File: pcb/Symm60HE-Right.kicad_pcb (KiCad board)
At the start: 2 copper layers, 157.9 x 105.9 mm, 114 parts

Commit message: Rename to Symm60HE; two-layer routing that is clean by construction
Rename every DOE60-* file and reference to Symm60HE-*, matching the repo.
The seven "DOE" mentions that remain are about the layout being reproduced,
which is correct.

Routing is now two layers with vias, at 0.2 mm trace / 0.15 mm clearance /
0.45 mm vias -- a rule chosen so the 0.5 mm grid's own diagonal spacing
(0.354 mm) satisfies it, and relaxed for any fabricator.

Three fixes, each of which was a real defect in the single-layer pass:

  * A diagonal step now requires both of its orthogonal neighbours.  Without
    it two nets cut the same gap from opposite corners and cross; cell
    ownership cannot see that, because neither net owns a cell the other
    used.  It was producing 49 shorts on the left half alone.
  * Fine-pitch pins are met head-on through a private escape lane along the
    pad's own axis, staggered near/far by pin parity.  A 0.65 mm TSSOP has
    0.25 mm between pads, so there is no side access at any rule; and without
    the lane the two neighbours' keep-out margins meet in front of a pin's
    tip and one of them owns the only way out.  The lane runs both ways,
    because an edge connector's contacts face off-board -- that is the way
    the cable goes in -- so its only exit is inwards under its own body.
  * Every route is rebuilt as real geometry and checked against everything
    already on the board before it is kept.  A route that would violate
    clearance is dropped and counted unrouted, so the files on disk are clean
    by construction and the honest number is the routed/unrouted split.

Left 143 of 156 connections, right 151 of 168, daughterboard 15 of 37.

Two things the checks were missing:

  * routecheck.py never tested trace-to-trace clearance, which is exactly
    what the diagonal crossings needed.  It does now, and it no longer counts
    a branch leaving its trunk at a T as a loose end.
  * The USB-C keep-out only existed in the image script -- nothin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
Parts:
- removed AML1, AML2, AML3, AML4: SN74LV4051A, DOE60_Project:AM1_TSSOP-16_4.4x5mm_P0.65mm
- removed CL10A, CL11A, CL12A, CL13A, CL14A, CL15A, CL16A, CL17A, CL18A, CL19A, CL1A, CL20A, CL21A, CL22A, CL23A, CL24A, CL25A, CL26A, CL27A, CL28A, CL29A, CL2A, CL30A, CL31A, CL32A, CL33A, CL3A, CL4A, CL5A, CL6A, CL7A, CL8A, CL9A, CML1, CML2, CML3, CML4: 100n, DOE60_Project:C1_C_0402_1005Metric
- removed CL10B, CL11B, CL12B, CL13B, CL14B, CL15B, CL16B, CL17B, CL18B, CL19B, CL1B, CL20B, CL21B, CL22B, CL23B, CL24B, CL25B, CL26B, CL27B, CL28B, CL29B, CL2B, CL30B, CL31B, CL32B, CL33B, CL3B, CL4B, CL5B, CL6B, CL7B, CL8B, CL9B: 4.7n, DOE60_Project:C1_C_0402_1005Metric
- removed HEL1, HEL10, HEL11, HEL12, HEL13, HEL14, HEL16, HEL17, HEL18, HEL19, HEL2, HEL20, HEL22, HEL23, HEL24, HEL25, HEL26, HEL27, HEL29, HEL3, HEL31, HEL4, HEL5, HEL6, HEL7, HEL9: MT9102ET, DOE60_Project:HE_KEY_1.00u
- removed HEL15: MT9102ET, DOE60_Project:HE_KEY_1.75u
- removed HEL21, HEL33: MT9102ET, DOE60_Project:HE_KEY_2.25u
- removed HEL28, HEL30, HEL32, HEL8: MT9102ET, DOE60_Project:HE_KEY_1.50u
- removed JL1: FFC_12P, DOE60_Project:FFC_12P_1.00mm_TopContact
- removed MHL1, MHL2, MHL3, MHL4: M2, DOE60_Project:MountingHole_2.2mm_M2_Pad
- removed SL1, SL2: STAB_MX, DOE60_Project:STABILIZER_MX_2U
- added AMR1: SN74LV4051A, Symm60HE_Project:AM1_TSSOP-16_4.4x5mm_P0.65mm, B.Cu at (181.7, 63.5)
- added AMR2: SN74LV4051A, Symm60HE_Project:AM1_TSSOP-16_4.4x5mm_P0.65mm, B.Cu at (207.2, 65.0)
- added AMR3: SN74LV4051A, Symm60HE_Project:AM1_TSSOP-16_4.4x5mm_P0.65mm, B.Cu at (245.7, 65.0)
- added AMR4: SN74LV4051A, Symm60HE_Project:AM1_TSSOP-16_4.4x5mm_P0.65mm, B.Cu at (276.7, 53.5)
- added CMR1: 100n, Symm60HE_Project:C1_C_0402_1005Metric, B.Cu at (189.2, 63.5)
- added CMR2: 100n, Symm60HE_Project:C1_C_0402_1005Metric, B.Cu at (218.2, 62.5)
- added CMR3: 100n, Symm60HE_Project:C1_C_0402_1005Metric, B.Cu at (256.2, 62.5)
- added CMR4: 100n, Symm60HE_Project:C1_C_0402_1005Metric, B.Cu at (284.2, 55.5)
- added CR10A: 100n, Symm60HE_Project:C1_C_0402_1005Metric, B.Cu at (255.3, 21.7)
- added CR10B: 4.7n, Symm60HE_Project:C1_C_0402_1005Metric, B.Cu at (268.5, 35.5)
- added CR11A: 100n, Symm60HE_Project:C1_C_0402_1005Metric, B.Cu at (279.1, 21.7)
- added CR11B: 4.7n, Symm60HE_Project:C1_C_0402_1005Metric, B.Cu at (292.4, 35.5)
- added CR12A: 100n, Symm60HE_Project:C1_C_0402_1005Metric, B.Cu at (217.0, 21.9)
- added CR12B: 4.7n, Symm60HE_Project:C1_C_0402_1005Metric, B.Cu at (230.4, 35.5)
- added CR13A: 100n, Symm60HE_Project:C1_C_0402_1005Metric, B.Cu at (196.5, 22.9)
- added CR13B: 4.7n, Symm60HE_Project:C1_C_0402_1005Metric, B.Cu at (210.5, 35.9)
- added CR14A: 100n, Symm60HE_Project:C1_C_0402_1005Metric, B.Cu at (175.1, 24.9)
- added CR14B: 4.7n, Symm60HE_Project:C1_C_0402_1005Metric, B.Cu at (189.7, 37.2)
- added CR15A: 100n, Symm60HE_Project:C1_C_0402_1005Metric, B.Cu at (154.7, 27.2)
- added CR15B: 4.7n, Symm60HE_Project:C1_C_0402_1005Metric, B.Cu at (169.4, 39.4)
- added CR16A: 100n, Symm60HE_Project:C1_C_0402_1005Metric, B.Cu at (232.5, 40.7)
- added CR16B: 4.7n, Symm60HE_Project:C1_C_0402_1005Metric, B.Cu at (245.7, 54.5)
- added CR17A: 100n, Symm60HE_Project:C1_C_0402_1005Metric, B.Cu at (251.5, 40.7)
- added CR17B: 4.7n, Symm60HE_Project:C1_C_0402_1005Metric, B.Cu at (264.7, 54.5)
- added CR18A: 100n, Symm60HE_Project:C1_C_0402_1005Metric, B.Cu at (277.7, 40.7)
- added CR18B: 4.7n, Symm60HE_Project:C1_C_0402_1005Metric, B.Cu at (290.9, 54.5)
- added CR19A: 100n, Symm60HE_Project:C1_C_0402_1005Metric, B.Cu at (213.1, 41.0)
- added CR19B: 4.7n, Symm60HE_Project:C1_C_0402_1005Metric, B.Cu at (226.6, 54.6)
- added CR1A: 100n, Symm60HE_Project:C1_C_0402_1005Metric, B.Cu at (224.8, 2.66)
- added CR1B: 4.7n, Symm60HE_Project:C1_C_0402_1005Metric, B.Cu at (238.1, 16.4)
- added CR20A: 100n, Symm60HE_Project:C1_C_0402_1005Metric, B.Cu at (192.3, 42.2)
- added CR20B: 4.7n, Symm60HE_Project:C1_C_0402_1005Metric, B.Cu at (206.4, 55.1)
- added CR21A: 100n, Symm60HE_Project:C1_C_0402_1005Metric, B.Cu at (170.9, 44.4)
- added CR21B: 4.7n, Symm60HE_Project:C1_C_0402_1005Metric, B.Cu at (185.5, 56.7)
- added CR22A: 100n, Symm60HE_Project:C1_C_0402_1005Metric, B.Cu at (227.7, 59.8)
- added CR22B: 4.7n, Symm60HE_Project:C1_C_0402_1005Metric, B.Cu at (240.9, 73.6)
- added CR23A: 100n, Symm60HE_Project:C1_C_0402_1005Metric, B.Cu at (246.8, 59.8)
- added CR23B: 4.7n, Symm60HE_Project:C1_C_0402_1005Metric, B.Cu at (260.0, 73.6)
- added CR24A: 100n, Symm60HE_Project:C1_C_0402_1005Metric, B.Cu at (265.8, 59.8)
- added CR24B: 4.7n, Symm60HE_Project:C1_C_0402_1005Metric, B.Cu at (279.0, 73.6)
- added CR25A: 100n, Symm60HE_Project:C1_C_0402_1005Metric, B.Cu at (277.7, 59.8)
- added CR25B: 4.7n, Symm60HE_Project:C1_C_0402_1005Metric, B.Cu at (290.9, 73.6)
- added CR26A: 100n, Symm60HE_Project:C1_C_0402_1005Metric, B.Cu at (287.2, 59.8)
- added CR26B: 4.7n, Symm60HE_Project:C1_C_0402_1005Metric, B.Cu at (300.4, 73.6)
- added CR27A: 100n, Symm60HE_Project:C1_C_0402_1005Metric, B.Cu at (208.0, 60.3)
- added CR27B: 4.7n, Symm60HE_Project:C1_C_0402_1005Metric, B.Cu at (221.7, 73.7)
- added CR28A: 100n, Symm60HE_Project:C1_C_0402_1005Metric, B.Cu at (186.9, 61.8)
- added CR28B: 4.7n, Symm60HE_Project:C1_C_0402_1005Metric, B.Cu at (201.2, 74.5)
- added CR29A: 100n, Symm60HE_Project:C1_C_0402_1005Metric, B.Cu at (165.7, 64.0)
- added CR29B: 4.7n, Symm60HE_Project:C1_C_0402_1005Metric, B.Cu at (180.4, 76.3)
- added CR2A: 100n, Symm60HE_Project:C1_C_0402_1005Metric, B.Cu at (243.9, 2.62)
- added CR2B: 4.7n, Symm60HE_Project:C1_C_0402_1005Metric, B.Cu at (257.1, 16.4)
- added CR30A: 100n, Symm60HE_Project:C1_C_0402_1005Metric, B.Cu at (246.8, 78.8)
- added CR30B: 4.7n, Symm60HE_Project:C1_C_0402_1005Metric, B.Cu at (260.0, 92.6)
- added CR31A: 100n, Symm60HE_Project:C1_C_0402_1005Metric, B.Cu at (251.5, 78.8)
- added CR31B: 4.7n, Symm60HE_Project:C1_C_0402_1005Metric, B.Cu at (264.7, 92.6)
- added CR32A: 100n, Symm60HE_Project:C1_C_0402_1005Metric, B.Cu at (265.8, 78.8)
- added CR32B: 4.7n, Symm60HE_Project:C1_C_0402_1005Metric, B.Cu at (279.0, 92.6)
- added CR33A: 100n, Symm60HE_Project:C1_C_0402_1005Metric, B.Cu at (280.1, 78.8)
- added CR33B: 4.7n, Symm60HE_Project:C1_C_0402_1005Metric, B.Cu at (293.3, 92.6)
- added CR34A: 100n, Symm60HE_Project:C1_C_0402_1005Metric, B.Cu at (284.9, 78.8)
- added CR34B: 4.7n, Symm60HE_Project:C1_C_0402_1005Metric, B.Cu at (298.1, 92.6)
- added CR35A: 100n, Symm60HE_Project:C1_C_0402_1005Metric, B.Cu at (208.2, 79.5)
- added CR35B: 4.7n, Symm60HE_Project:C1_C_0402_1005Metric, B.Cu at (221.8, 92.9)
- added CR36A: 100n, Symm60HE_Project:C1_C_0402_1005Metric, B.Cu at (169.7, 82.8)
- added CR36B: 4.7n, Symm60HE_Project:C1_C_0402_1005Metric, B.Cu at (184.3, 95.1)
- added CR3A: 100n, Symm60HE_Project:C1_C_0402_1005Metric, B.Cu at (263.0, 2.62)
- added CR3B: 4.7n, Symm60HE_Project:C1_C_0402_1005Metric, B.Cu at (276.2, 16.4)
- added CR4A: 100n, Symm60HE_Project:C1_C_0402_1005Metric, B.Cu at (272.5, 2.62)
- added CR4B: 4.7n, Symm60HE_Project:C1_C_0402_1005Metric, B.Cu at (285.7, 16.4)
- added CR5A: 100n, Symm60HE_Project:C1_C_0402_1005Metric, B.Cu at (282.0, 2.62)
- added CR5B: 4.7n, Symm60HE_Project:C1_C_0402_1005Metric, B.Cu at (295.2, 16.4)
- added CR6A: 100n, Symm60HE_Project:C1_C_0402_1005Metric, B.Cu at (204.9, 3.29)
- added CR6B: 4.7n, Symm60HE_Project:C1_C_0402_1005Metric, B.Cu at (218.6, 16.6)
- added CR7A: 100n, Symm60HE_Project:C1_C_0402_1005Metric, B.Cu at (183.7, 4.93)
- added CR7B: 4.7n, Symm60HE_Project:C1_C_0402_1005Metric, B.Cu at (198.0, 17.5)
- added CR8A: 100n, Symm60HE_Project:C1_C_0402_1005Metric, B.Cu at (162.6, 7.24)
- added CR8B: 4.7n, Symm60HE_Project:C1_C_0402_1005Metric, B.Cu at (177.3, 19.5)
- added CR9A: 100n, Symm60HE_Project:C1_C_0402_1005Metric, B.Cu at (236.3, 21.7)
- added CR9B: 4.7n, Symm60HE_Project:C1_C_0402_1005Metric, B.Cu at (249.5, 35.5)
- added HER1: MT9102ET, Symm60HE_Project:HE_KEY_1.00u, B.Cu at (231.4, 9.54)
- added HER10: MT9102ET, Symm60HE_Project:HE_KEY_1.00u, B.Cu at (261.9, 28.6)
- added HER11: MT9102ET, Symm60HE_Project:HE_KEY_1.50u, B.Cu at (285.8, 28.6)
- added HER12: MT9102ET, Symm60HE_Project:HE_KEY_1.00u, B.Cu at (223.7, 28.7)
- added HER13: MT9102ET, Symm60HE_Project:HE_KEY_1.00u, B.Cu at (203.5, 29.4)
- added HER14: MT9102ET, Symm60HE_Project:HE_KEY_1.00u, B.Cu at (182.4, 31.1)
- added HER15: MT9102ET, Symm60HE_Project:HE_KEY_1.00u, B.Cu at (162.0, 33.3)
- added HER16: MT9102ET, Symm60HE_Project:HE_KEY_1.00u, B.Cu at (239.1, 47.6)
- added HER17: MT9102ET, Symm60HE_Project:HE_KEY_1.00u, B.Cu at (258.1, 47.6)
- added HER18: MT9102ET, Symm60HE_Project:HE_KEY_1.75u, B.Cu at (284.3, 47.6)
- added HER19: MT9102ET, Symm60HE_Project:HE_KEY_1.00u, B.Cu at (219.8, 47.8)
- added HER2: MT9102ET, Symm60HE_Project:HE_KEY_1.00u, B.Cu at (250.5, 9.53)
- added HER20: MT9102ET, Symm60HE_Project:HE_KEY_1.00u, B.Cu at (199.3, 48.7)
- added HER21: MT9102ET, Symm60HE_Project:HE_KEY_1.00u, B.Cu at (178.2, 50.5)
- added HER22: MT9102ET, Symm60HE_Project:HE_KEY_1.00u, B.Cu at (234.3, 66.7)
- added HER23: MT9102ET, Symm60HE_Project:HE_KEY_1.00u, B.Cu at (253.4, 66.7)
- added HER24: MT9102ET, Symm60HE_Project:HE_KEY_1.00u, B.Cu at (272.4, 66.7)
- added HER25: MT9102ET, Symm60HE_Project:HE_KEY_2.25u, B.Cu at (284.3, 66.7)
- added HER26: MT9102ET, Symm60HE_Project:HE_KEY_1.25u, B.Cu at (293.8, 66.7)
- added HER27: MT9102ET, Symm60HE_Project:HE_KEY_1.00u, B.Cu at (214.8, 67.0)
- added HER28: MT9102ET, Symm60HE_Project:HE_KEY_1.00u, B.Cu at (194.0, 68.1)
- added HER29: MT9102ET, Symm60HE_Project:HE_KEY_1.00u, B.Cu at (173.0, 70.2)
- added HER3: MT9102ET, Symm60HE_Project:HE_KEY_1.00u, B.Cu at (269.6, 9.53)
- added HER30: MT9102ET, Symm60HE_Project:HE_KEY_1.00u, B.Cu at (253.4, 85.7)
- added HER31: MT9102ET, Symm60HE_Project:HE_KEY_1.50u, B.Cu at (258.1, 85.7)
- added HER32: MT9102ET, Symm60HE_Project:HE_KEY_1.00u, B.Cu at (272.4, 85.7)
- added HER33: MT9102ET, Symm60HE_Project:HE_KEY_1.50u, B.Cu at (286.7, 85.7)
- added HER34: MT9102ET, Symm60HE_Project:HE_KEY_1.00u, B.Cu at (291.5, 85.7)
- added HER35: MT9102ET, Symm60HE_Project:HE_KEY_1.50u, B.Cu at (215.0, 86.2)
- added HER36: MT9102ET, Symm60HE_Project:HE_KEY_2.25u, B.Cu at (177.0, 89.0)
- added HER4: MT9102ET, Symm60HE_Project:HE_KEY_2.00u, B.Cu at (279.1, 9.53)
- added HER5: MT9102ET, Symm60HE_Project:HE_KEY_1.00u, B.Cu at (288.6, 9.53)
- added HER6: MT9102ET, Symm60HE_Project:HE_KEY_1.00u, B.Cu at (211.8, 9.93)
- added HER7: MT9102ET, Symm60HE_Project:HE_KEY_1.00u, B.Cu at (190.8, 11.2)
- added HER8: MT9102ET, Symm60HE_Project:HE_KEY_1.00u, B.Cu at (169.9, 13.3)
- added HER9: MT9102ET, Symm60HE_Project:HE_KEY_1.00u, B.Cu at (242.9, 28.6)
- added JR1: FFC_12P, Symm60HE_Project:FFC_12P_1.00mm_TopContact, B.Cu at (164.2, 48.5)
- added MHR1: M2, Symm60HE_Project:MountingHole_2.2mm_M2_Pad, F.Cu at (163.2, 10.5)
- added MHR2: M2, Symm60HE_Project:MountingHole_2.2mm_M2_Pad, F.Cu at (166.2, 89.5)
- added MHR3: M2, Symm60HE_Project:MountingHole_2.2mm_M2_Pad, F.Cu at (295.2, 9.52)
- added MHR4: M2, Symm60HE_Project:MountingHole_2.2mm_M2_Pad, F.Cu at (298.2, 88.0)
- added SR1: STAB_MX, Symm60HE_Project:STABILIZER_MX_2U, F.Cu at (279.1, 9.53)
- added SR2: STAB_MX, Symm60HE_Project:STABILIZER_MX_2U, F.Cu at (284.3, 66.7)
- added SR3: STAB_MX, Symm60HE_Project:STABILIZER_MX_2U, F.Cu at (177.0, 89.0)
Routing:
- net +3V3A: track 332.8 -> 904.7 mm, vias 33 -> 53
- net HE_R05: track 0.00 -> 151.9 mm, vias 0 -> 2
- net MUX_A0: track 0.00 -> 143.1 mm, vias 0 -> 6
- net ADC_R4: track 0.00 -> 128.6 mm, vias 0 -> 2
- net HE_R27: track 0.00 -> 125.2 mm, vias 0 -> 2
- net HE_R32: track 0.00 -> 118.7 mm, vias 0 -> 2
- net HE_R03: track 0.00 -> 103.8 mm, vias 0 -> 2
- net HE_R26: track 0.00 -> 95.5 mm, vias 0 -> 2
- net ADC_R3: track 0.00 -> 90.6 mm, vias 0 -> 2
- net HE_R28: track 0.00 -> 85.9 mm, vias 0 -> 2
- net HE_R02: track 0.00 -> 85.7 mm, vias 0 -> 2
- net HE_R11: track 0.00 -> 81.4 mm, vias 0 -> 2
- net HE_R01: track 0.00 -> 72.0 mm, vias 0 -> 2
- net HE_R06: track 0.00 -> 68.6 mm, vias 0 -> 2
- net HE_R30: track 0.00 -> 65.3 mm
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- added copper zone on F.Cu, net GND
- removed copper zone on F.Cu, net +3V3A
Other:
- board size 157.9 x 105.9 mm -> 155.5 x 106.4 mm

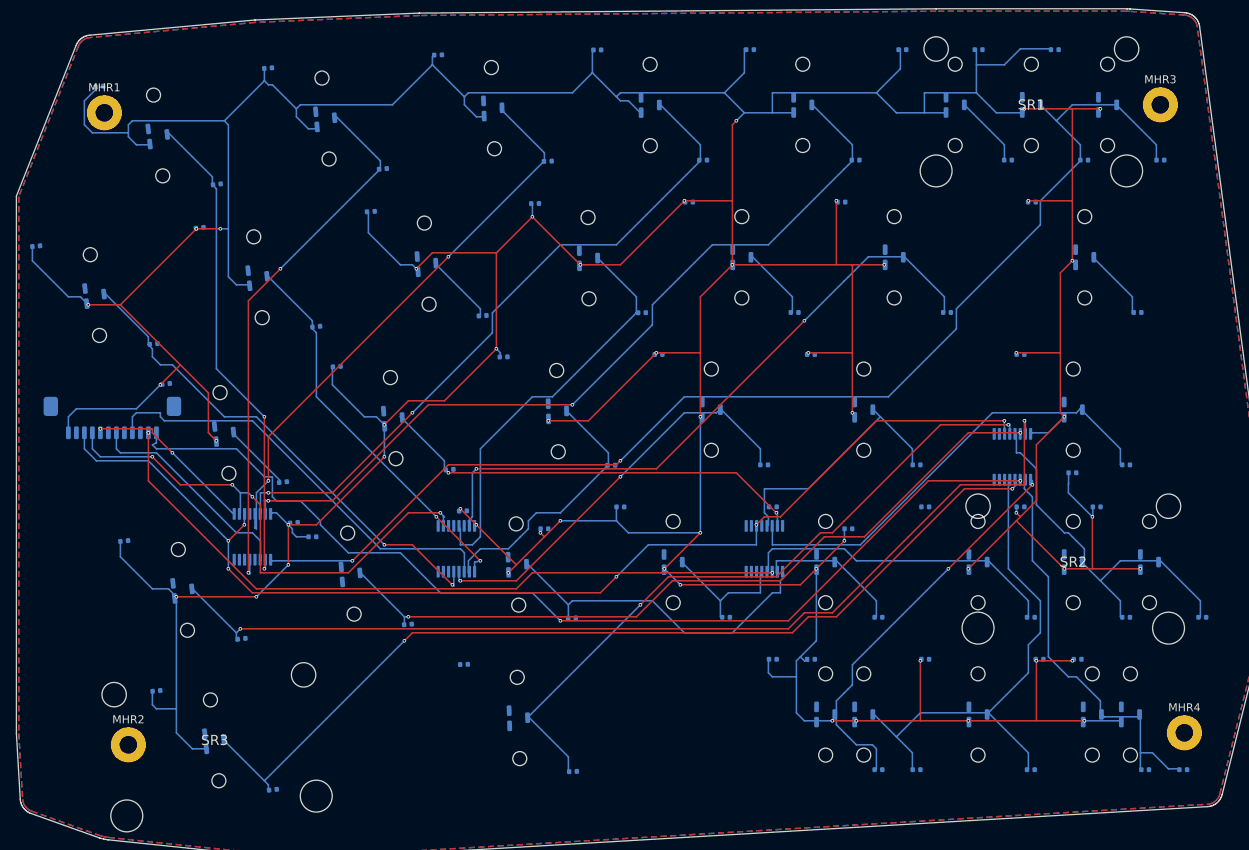
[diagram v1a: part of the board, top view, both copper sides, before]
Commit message: Get the boards routing: SOIC muxes, FN40HE's pinout, a rail plane
Four changes, none of which touch what the circuit is made of.

SOIC-16 muxes.  FN40HE fits the SN74LV4051A in TSSOP-16, and every remaining
failure on the halves was an interior pin of one.  A 0.65 mm pitch leaves
0.25 mm between pads: no trace fits between them at any rule a fabricator
will take, so those pins could only ever escape by via through a gap their
neighbours already owned.  Same chip in SOIC-16 -- SN74LV4051AD -- has
1.27 mm pitch and 0.67 mm between pads, which a 0.2 mm trace clears with
0.15 mm either side.  It costs about 30 mm2 a package on boards that have
room under the keycaps, and it hand solders.

The MCU pin assignment is FN40HE's again, read off its board: crystal on
5/6, reset on 7, the mux selects on 9/10/11, the analog rail on 13, the
eight multiplexed inputs on 17 and 20-26, USB and its reference resistor on
33/34/35, SWD on 46/49/55, boot on 60.  The previous commit had moved those
around to suit the layout, which is backwards -- most of them are fixed in
silicon.  The parts move instead.  NOTICE.md is corrected accordingly.

The analog rail is a pour, not a net.  It reaches 75 pads on the left half;
routed as traces it is a spanning tree that gets there first and walls off
the three select lines, which have one shape that works.  F.Cu carries it
instead -- the halves have no components on the front -- and each rail pad
taps it through a via of its own.  That is FN40HE's +3.3VA zone, on the
other side because our board is populated the other way up.  B.Cu stays the
GND pour, so neither rail is routed.

And the one that mattered most: a pad's list of ways to be met had the bare
pad centre first.  Meeting a pad in its middle lets the maze leave sideways,
which on a 0.5 mm pitch package crosses the neighbouring pin, so all twelve
of those candidates were found and then thrown out by the clearance check --
exhausting the per-pad budget before the escapes along the pad's own a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
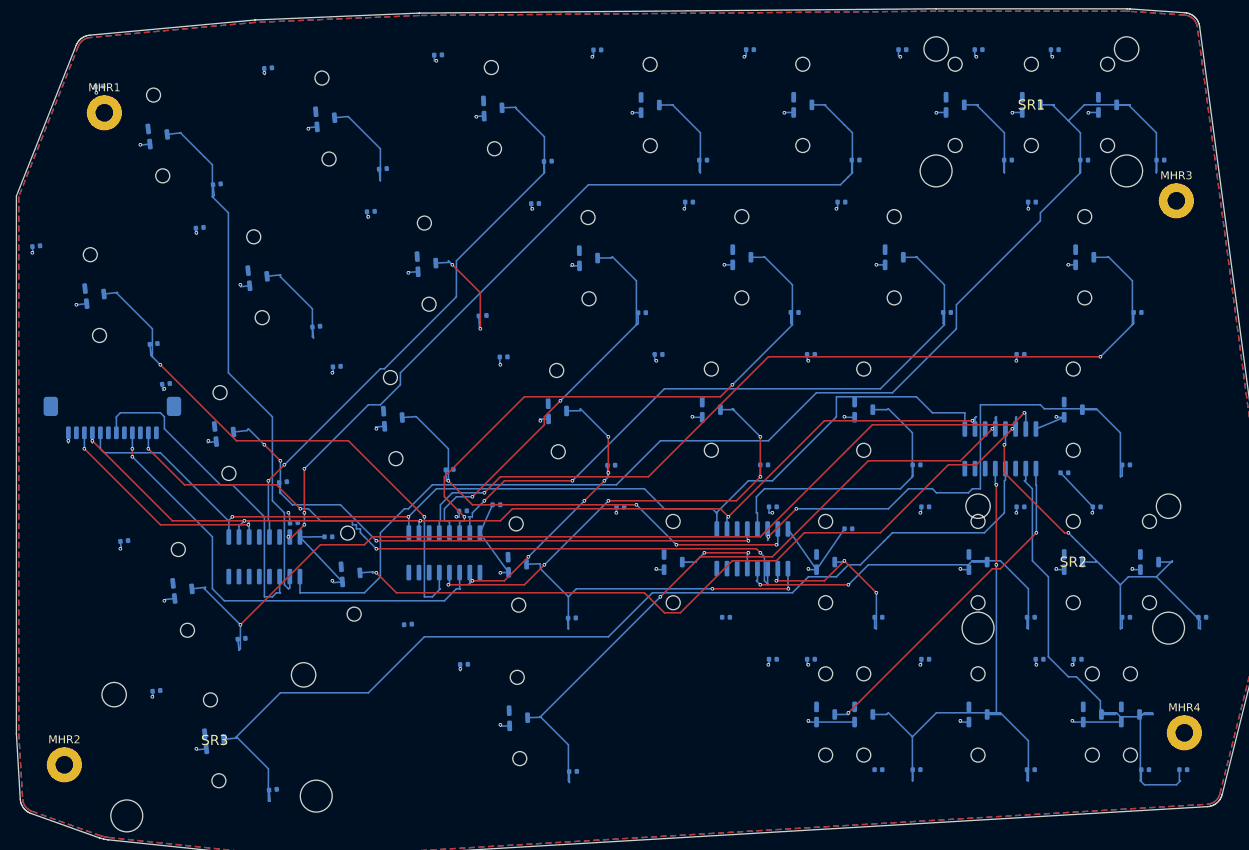
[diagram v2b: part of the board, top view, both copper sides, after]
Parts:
- AMR1, AMR2, AMR3, AMR4: footprint Symm60HE_Project:AM1_TSSOP-16_4.4x5mm_P0.65mm -> Symm60HE_Project:AM1_SOIC-16_3.9x9.9mm_P1.27mm
- moved MHR3 12.2 mm to (297.2, 21.5)
- moved MHR2 8.38 mm to (158.2, 92.0)
- moved CMR2 6.71 mm to (212.2, 59.5)
- moved AMR1 2.92 mm to (183.2, 66.0)
- moved CMR1 2.00 mm to (191.2, 63.5)
- moved AMR4 1.80 mm to (275.2, 52.5)
- moved AMR2 1.58 mm to (205.7, 65.5)
- moved AMR3 1.50 mm to (244.2, 65.0)
- moved CMR4 1.00 mm to (283.2, 55.5)
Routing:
- net +3V3A: track 904.7 -> 131.4 mm, vias 53 -> 71
- net ADC_R4: track 128.6 -> 0.00 mm, vias 2 -> 0
- net MUX_A0: track 143.1 -> 29.1 mm, vias 6 -> 2
- net MUX_A2: track 21.9 -> 133.2 mm
- net HE_R12: track 9.42 -> 112.6 mm, vias 0 -> 2
- net HE_R02: track 85.7 -> 13.4 mm, vias 2 -> 0
- net HE_R20: track 8.92 -> 75.6 mm, vias 0 -> 4
- net MUX_A1: track 64.7 -> 129.6 mm, vias 4 -> 5
- net HE_R10: track 9.47 -> 73.3 mm, vias 0 -> 2
- net HE_R06: track 68.6 -> 12.9 mm, vias 2 -> 0
- net HE_R13: track 48.8 -> 12.7 mm, vias 2 -> 0
- net ADC_R1: track 27.4 -> 41.3 mm
- net HE_R18: track 57.8 -> 69.7 mm, vias 0 -> 2
- net HE_R05: track 151.9 -> 162.2 mm, vias 2 -> 0
- net HE_R31: track 52.5 -> 62.1 mm
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- added copper zone on F.Cu, net +3V3A
- removed copper zone on F.Cu, net GND
